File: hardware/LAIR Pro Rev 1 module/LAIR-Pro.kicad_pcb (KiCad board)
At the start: 2 copper layers, 103.1 x 49.9 mm, 12 parts, among them J1 Conn_02x10_Odd_Even, J2 Conn_02x10_Odd_Even, J3 Conn_02x10_Odd_Even, J4 Conn_02x10_Odd_Even, J5 RC2014_Pro_Bus, J6 RC2014_Pro_Bus, J7 Conn_02x05_Odd_Even, U1 74LS240, U2 74LS244

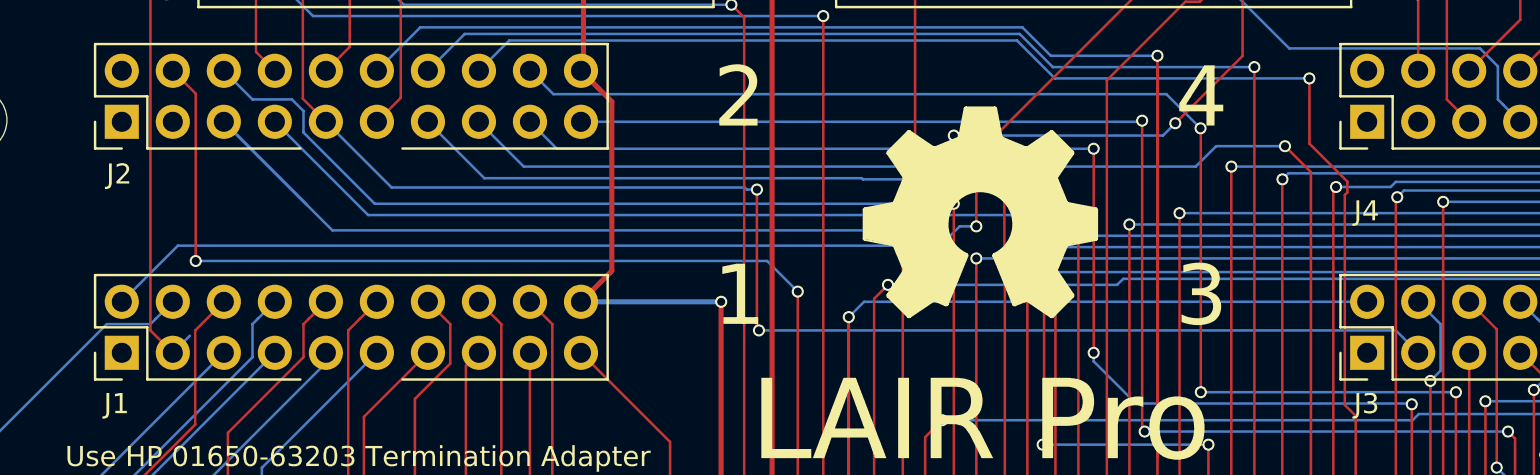
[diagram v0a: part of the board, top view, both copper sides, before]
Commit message: Use only one clock input per pod
The documentation for the HP Termination Adapter calls out
two clock signals on each adapter, but the actual pods on
the logic analyzers have only one clock per pod, which is
on pin3 of the Termination Adapter. Pin 2 is unused.
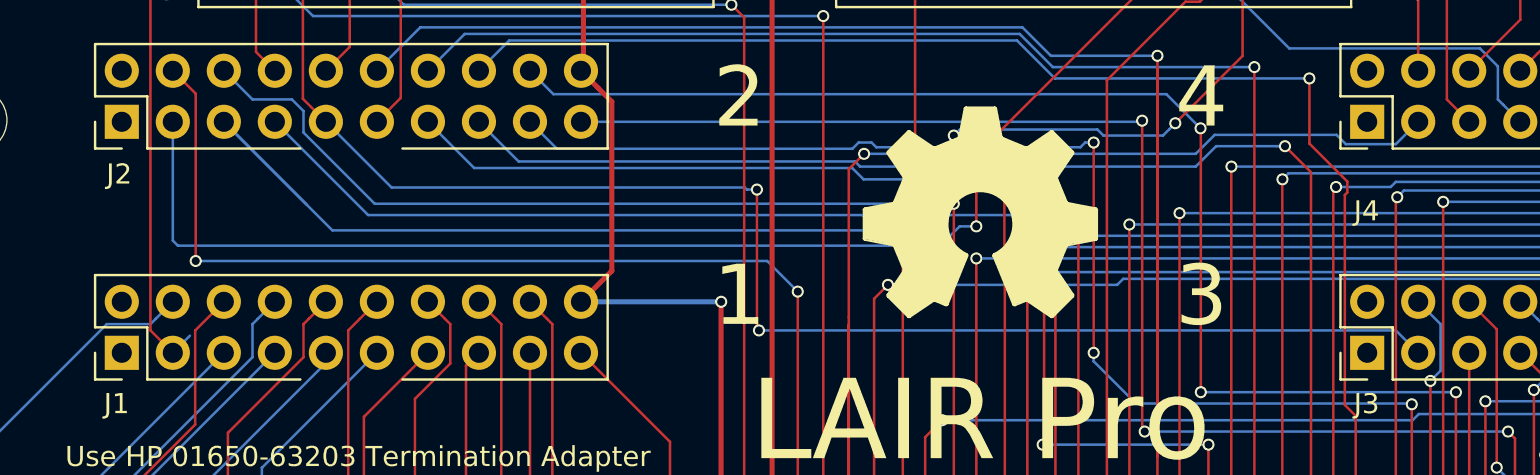
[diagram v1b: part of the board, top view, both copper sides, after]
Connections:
- J1 pad 2: /K_CLK -> (no net)
- J2 pad 3: (no net) -> /K_CLK
- J3 pad 2: /CLOCK -> (no net)
- J4 pad 3: (no net) -> /CLOCK
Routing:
- net /CLOCK: track 60.4 -> 71.4 mm
- net /K_CLK: track 72.6 -> 74.9 mm
- net /D2: track 76.6 -> 77.2 mm

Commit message: Put the product name on the back silkscreen
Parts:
- added ?: , graphics:LAIR, F.Cu at (214.6, 128.3)

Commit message: Adjust timing to account for HP's buffering everything
On the HP Z80 adapter, they buffer the address bus, the data bus,
and every other signal through a 74LS241. They then have to add
more delay to WR and IORQ to make the timing work, and for some
reason they invert WR while they're at it.

We don't have room to buffer everything, so we can't follow HP's
design without expanding the board beyond the RC-2014 form factor.
Since we aren't buffering ADDR or DATA, we can't add delays to
the other control signals, either. We just need to add the extra
delays on WR and IORQ. We keep WR inverted for compatibility.

The HP Z80 adapter also inverts IORQ and MREQ for use as the clocks
of the state analyzer. I don't know why. We can't invert them (that
would add unwanted delay), so the user will need to configure the
Master Clock for rising edges on J and K, rather than falling edges
as with the HP adapter.

This change leaves most of U1 and U2 unused. The data sheet says
we need to tie off the unused inputs. They are now tied to ground
through individual visible traces on the back side, so they can
be cut if the gates are needed for mods.
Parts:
- moved ? 1.27 mm to (213.4, 128.3)
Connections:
- J1 pad 3: /J_CLK -> /MREQ
- J2 pad 3: /K_CLK -> /IORQ
- J2 pad 8: /XM1 -> /M1
- J2 pad 9: /XRFSH -> /RFSH
- J3 pad 3: /XRFSH -> /RFSH
- U1 pad 11: /K_CLK -> GND
- U1 pad 12: /K_CLK -> (no net)
- U1 pad 13: /MREQ -> GND
- U1 pad 14: /XWR -> (no net)
- U1 pad 16: Net-(U1-Pad16) -> (no net)
- U1 pad 4: Net-(U1-Pad18) -> GND
- U1 pad 6: Net-(U1-Pad16) -> GND
- U1 pad 7: /J_CLK -> (no net)
- U1 pad 8: /IORQ -> GND
- U1 pad 9: /XIORQ -> (no net)
- U2 pad 16: /XM1 -> /XIORQ
- U2 pad 18: /XRFSH -> /XWR
- U2 pad 2: /RFSH -> Net-(U1-Pad18)
- U2 pad 4: /M1 -> /IORQ
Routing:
- net /XRFSH: track 78.9 -> 0.00 mm, vias 2 -> 0
- net /J_CLK: track 77.6 -> 0.00 mm, vias 2 -> 0
- net /K_CLK: track 74.9 -> 0.00 mm, vias 2 -> 0
- net /IORQ: track 63.3 -> 117.2 mm, vias 0 -> 3
- net GND: track 207.1 -> 253.2 mm, vias 2 -> 0
- net /XIORQ: track 53.4 -> 14.3 mm, vias 1 -> 0
- net /XWR: track 52.9 -> 17.7 mm, vias 2 -> 0
- net Net-(U1-Pad18): track 8.67 -> 38.5 mm
- net /MREQ: track 101.8 -> 80.8 mm, vias 3 -> 1
- net /RFSH: track 62.9 -> 83.8 mm, vias 1 -> 2
- net /XM1: track 18.0 -> 0.00 mm, vias 1 -> 0
- net Net-(U1-Pad16): track 8.67 -> 0.00 mm
- net /RESET: track 66.9 -> 65.4 mm
- net /M1: track 58.9 -> 57.6 mm
